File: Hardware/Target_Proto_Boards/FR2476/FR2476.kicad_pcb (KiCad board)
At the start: 2 copper layers, 70 x 40 mm, 44 parts, among them J1 USB_B_Micro, J10 PORT6, J11 PORT3, J12 JTAG/SBW, J13 VSEL, J14 VCC, J15 GND, J16 +5V, J17 GND, J4 LED_P4.1, J5 DEBUG, J6 PORT4, J7 PORT1, J8 PORT5, J9 PORT2, SW1 TL-2203, SW2 RESET, U1 MSP430FR2476TPTR, U2 HT7533-1, Y1 32768 12pF

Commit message: Updated Hardware Schematics and Boards
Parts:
- removed RN1, RN2: 4x470, lib:R_Array_Convex_4x0603_handsoldered
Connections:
- J12 pad 3: /JTDI -> /P1.6_TDI
- J12 pad 5: /JTMS -> /P1.5_TDO
- J5 pad 1: /RTDO -> /JTDO
- J5 pad 11: /RRST -> /JRST
- J5 pad 13: /RTEST -> /JTEST
- J5 pad 3: /RTCK -> /JTCK
- J5 pad 5: /RRST -> /JRST
- J5 pad 7: /RTDO -> /JTDO
- J5 pad 9: /RTCK -> /JTCK
- J7 pad 6: /P1.5 -> /P1.5_TDO
- J7 pad 7: /P1.6 -> /P1.6_TDI
- J8 pad 2: /P5.1 -> /JRXD
- J8 pad 3: /P5.2 -> /JTXD
- U1 pad 44: /P5.1 -> /JRXD
- U1 pad 45: /P5.2 -> /JTXD
- U1 pad 5: /P1.5 -> /P1.5_TDO
- U1 pad 6: /P1.6 -> /P1.6_TDI
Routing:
- net /JRXD: track 6.42 -> 68.4 mm, vias 0 -> 2
- net /P5.1: track 60.5 -> 0.00 mm, vias 2 -> 0
- net /JTXD: track 12.2 -> 72.5 mm, vias 0 -> 2
- net /P5.2: track 58.3 -> 0.00 mm, vias 2 -> 0
- net /P1.5_TDO: track 0.00 -> 57.4 mm, vias 0 -> 4
- net /P1.6_TDI: track 0.00 -> 55.2 mm, vias 0 -> 4
- net /P1.5: track 47.3 -> 0.00 mm, vias 4 -> 0
- net /P1.6: track 44.4 -> 0.00 mm, vias 4 -> 0
- net /JTCK: track 7.86 -> 21.8 mm, vias 0 -> 2
- net /JTDO: track 10.4 -> 24.2 mm
- net /JRST: track 14.8 -> 28.4 mm
- net /RTCK: track 12.2 -> 0.00 mm
- net /RTDO: track 11.9 -> 0.00 mm
- net /RRST: track 11.7 -> 0.00 mm
- net /JTDI: track 8.85 -> 0.00 mm
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
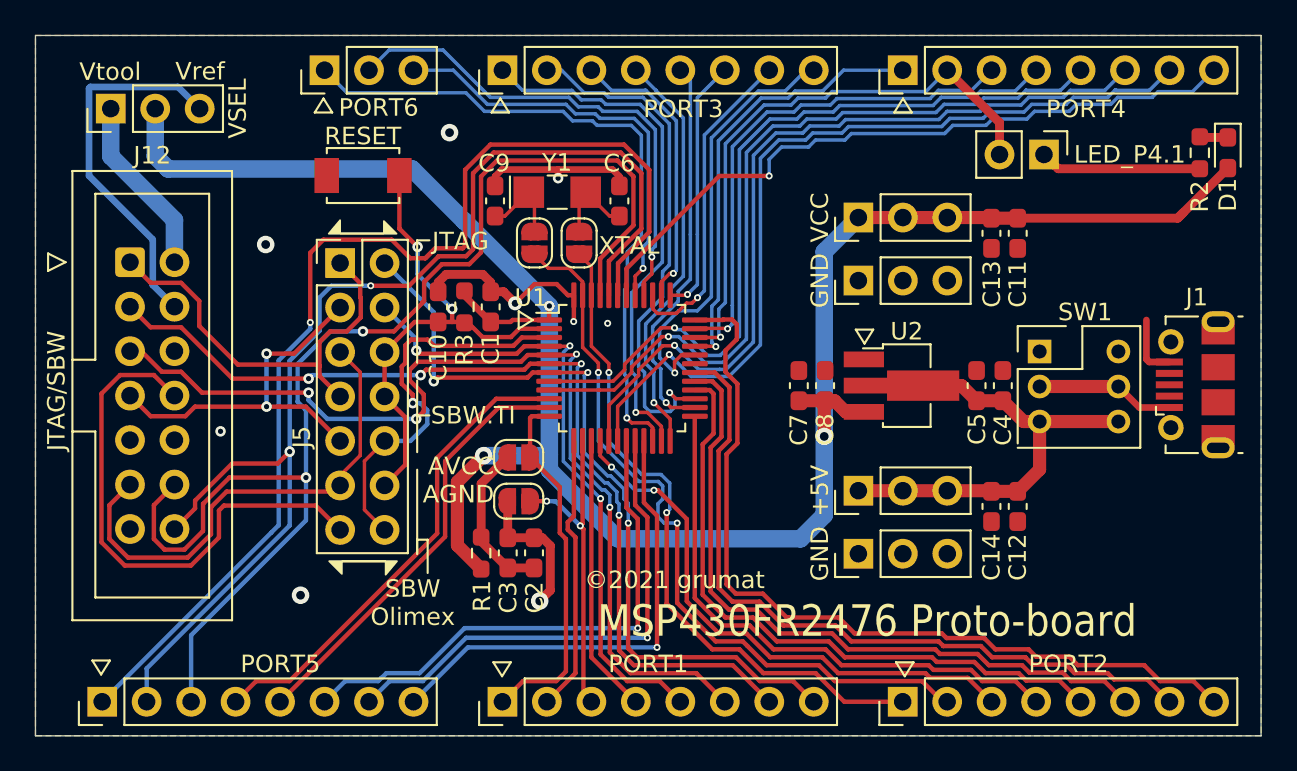
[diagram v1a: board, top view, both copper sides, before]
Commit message: Documentation for the MSP430FR2476 Proto board
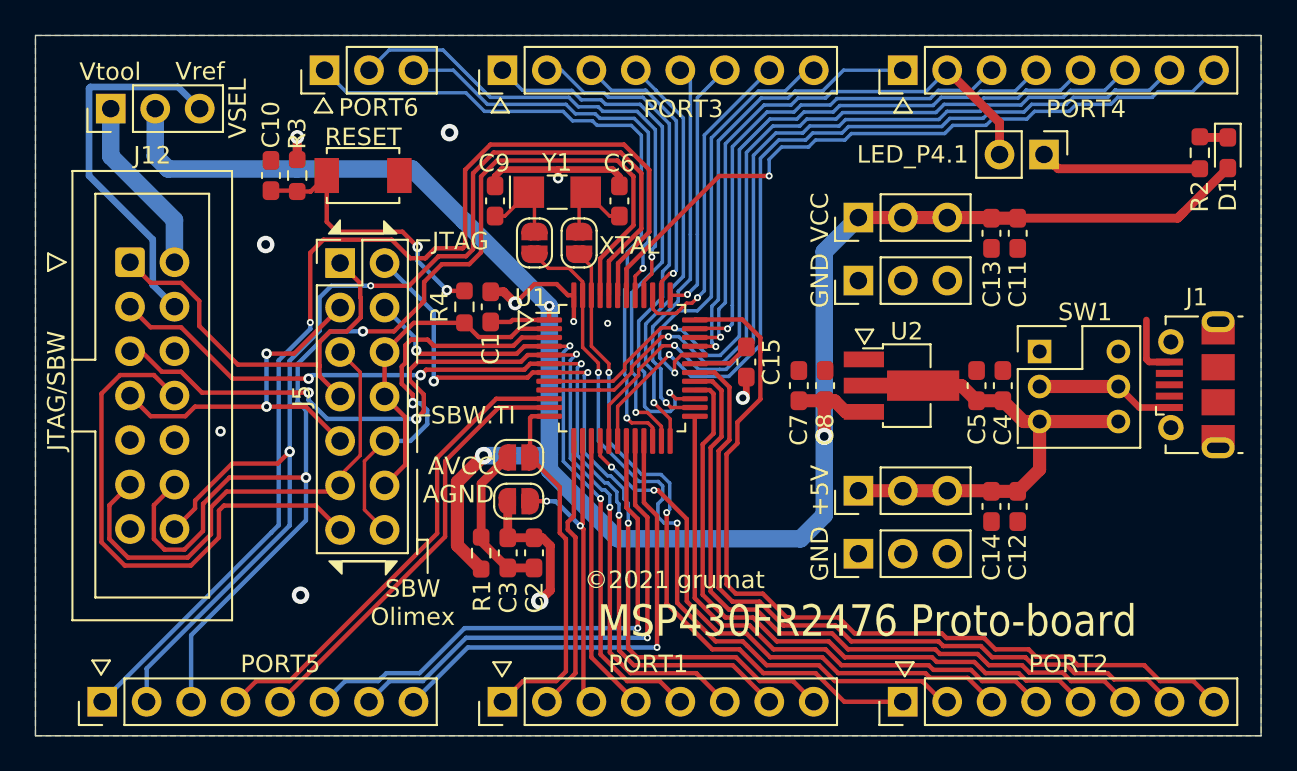
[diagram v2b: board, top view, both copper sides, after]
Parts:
- added C15: 1uF, Capacitor_SMD:C_0603_1608Metric_Pad1.08x0.95mm_HandSolder, F.Cu at (148.6, 101.7)
- added R4: 3.3K, Resistor_SMD:R_0603_1608Metric_Pad0.98x0.95mm_HandSolder, F.Cu at (132.5, 98.5)
- C10: value 1nF -> 2.2nF
- moved C10 12.1 mm to (121.5, 91.0)
- moved R3 12.1 mm to (123.0, 91.0)
- turned SW2 to 0 degrees
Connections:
- C10 pad 1: /RESET -> Net-(C10-Pad1)
- R3 pad 2: /RESET -> Net-(C10-Pad1)
- SW2 pad 1: /RESET -> Net-(C10-Pad1)
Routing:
- net Net-(C10-Pad1): track 0.00 -> 16.2 mm, vias 0 -> 2
- net /RESET: track 28.9 -> 19.2 mm, vias 2 -> 0
- net Net-(C15-Pad1): track 0.00 -> 3.34 mm
- net GND: track 32.7 -> 29.5 mm, vias 9 -> 10
- net /P2.7: track 48.8 -> 49.9 mm
- net +3V3: track 120.6 -> 121.3 mm, vias 3 -> 4

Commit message: Updated FR2476 proto board
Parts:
- J5: footprint Connector_PinHeader_2.54mm:PinHeader_2x07_P2.54mm_Vertical -> Connector_PinHeader_2.54mm:PinHeader_2x06_P2.54mm_Vertical
- U2: value HT7533-1 -> AMS1117-3.3
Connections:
- net +3V3 renamed +3.3V
- J1 pad 2: Net-(J1-Pad2) -> unconnected-(J1-Pad2)
- J1 pad 3: Net-(J1-Pad3) -> unconnected-(J1-Pad3)
- J1 pad 4: Net-(J1-Pad4) -> unconnected-(J1-Pad4)
- J12 pad 10: Net-(J12-Pad10) -> unconnected-(J12-Pad10)
- J12 pad 6: Net-(J12-Pad6) -> unconnected-(J12-Pad6)
- J5 pad 11: /JRST -> /JTDO
- J5 pad 7: /JTDO -> /JTEST
- J5 pad 8: /RESET -> /TEST
- SW1 pad 1: Net-(SW1-Pad1) -> unconnected-(SW1-Pad1)
- SW1 pad 4: Net-(SW1-Pad4) -> unconnected-(SW1-Pad4)
- U1 pad 44: /JRXD -> /JTXD
- U1 pad 45: /JTXD -> /JRXD
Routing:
- net /JTEST: track 30.7 -> 10.1 mm
- net /TEST: track 23.0 -> 14.6 mm, vias 1 -> 0
- net /P1.6_TDI: track 55.2 -> 60.1 mm, vias 4 -> 3
- net /JTCK: track 21.8 -> 25.3 mm, vias 2 -> 0
- net /JTDO: track 24.2 -> 27.5 mm
- net /JTXD: track 72.5 -> 69.3 mm
- net /P5.0: track 65.2 -> 62.4 mm
- net /JRXD: track 68.4 -> 66.4 mm
- net /JRST: track 28.4 -> 29.0 mm
- net GND: track 29.5 -> 30.1 mm, vias 10 -> 11
- net /P1.5_TDO: track 57.4 -> 57.3 mm, vias 4 -> 3
- net Net-(C10-Pad1): vias 2 -> 0
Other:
- net class Default removed
- net class Power removed
- board text added: "DIO"
- board text added: "RST"
- board text added: "TCK"
- board text added: "TDO"
- board text added: "TEST"
- board text added: "©2022 grumat"
- board text removed: "SBW Olimex"
- board text removed: "©2021 grumat"
